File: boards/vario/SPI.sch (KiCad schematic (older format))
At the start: 21 parts, among them Q4 Q_PMOS_DGS, U1 74HC273, U2 74LS161, U3 74HC74, U31 74LS14, U32 74LS32, U33 74LS08, U4 74HC273, U5 74LS151, U6 74HC244

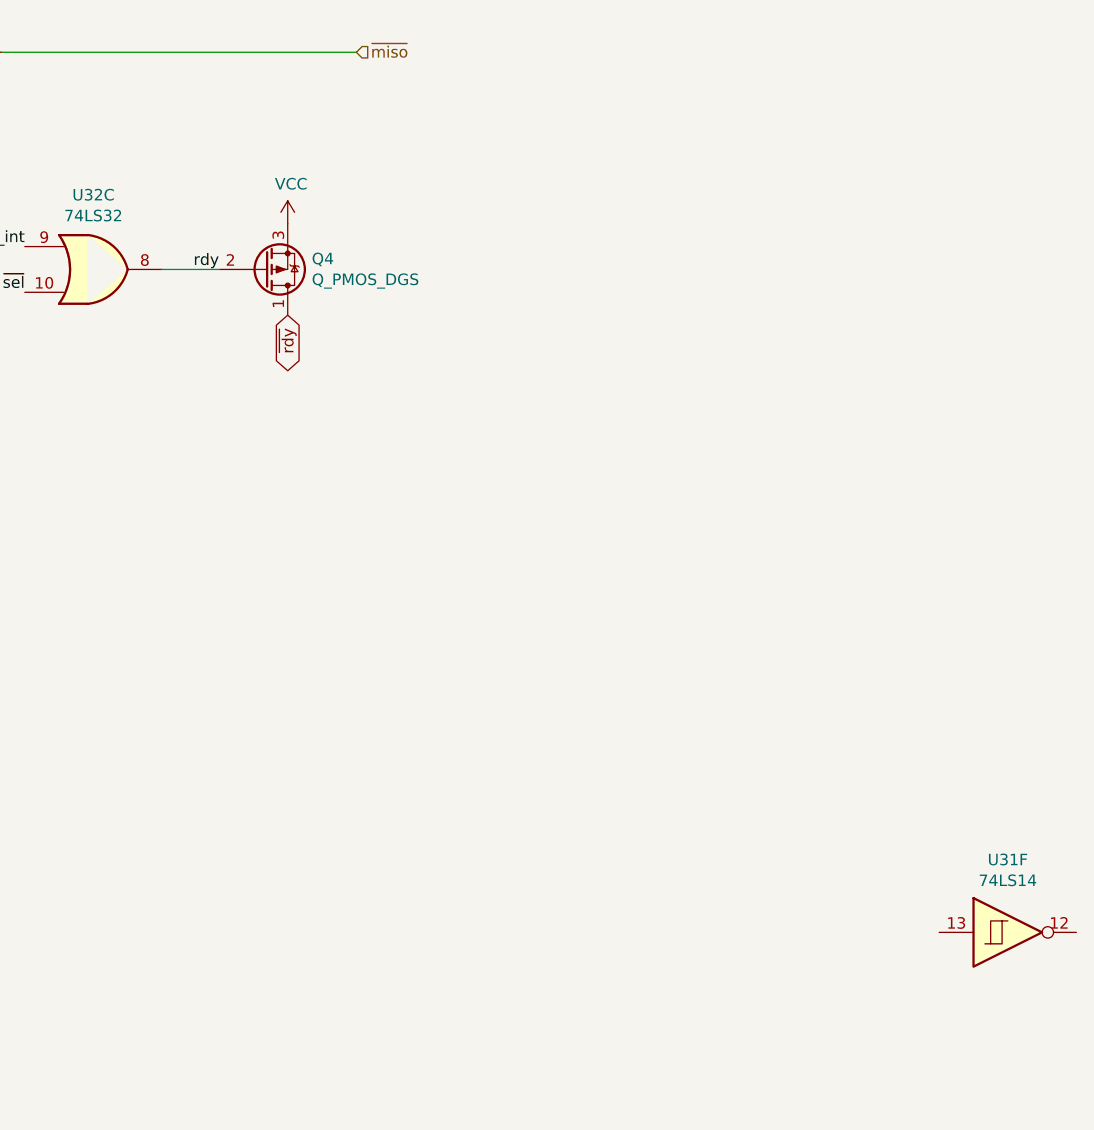
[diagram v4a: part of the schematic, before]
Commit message: SPI: invert RDY
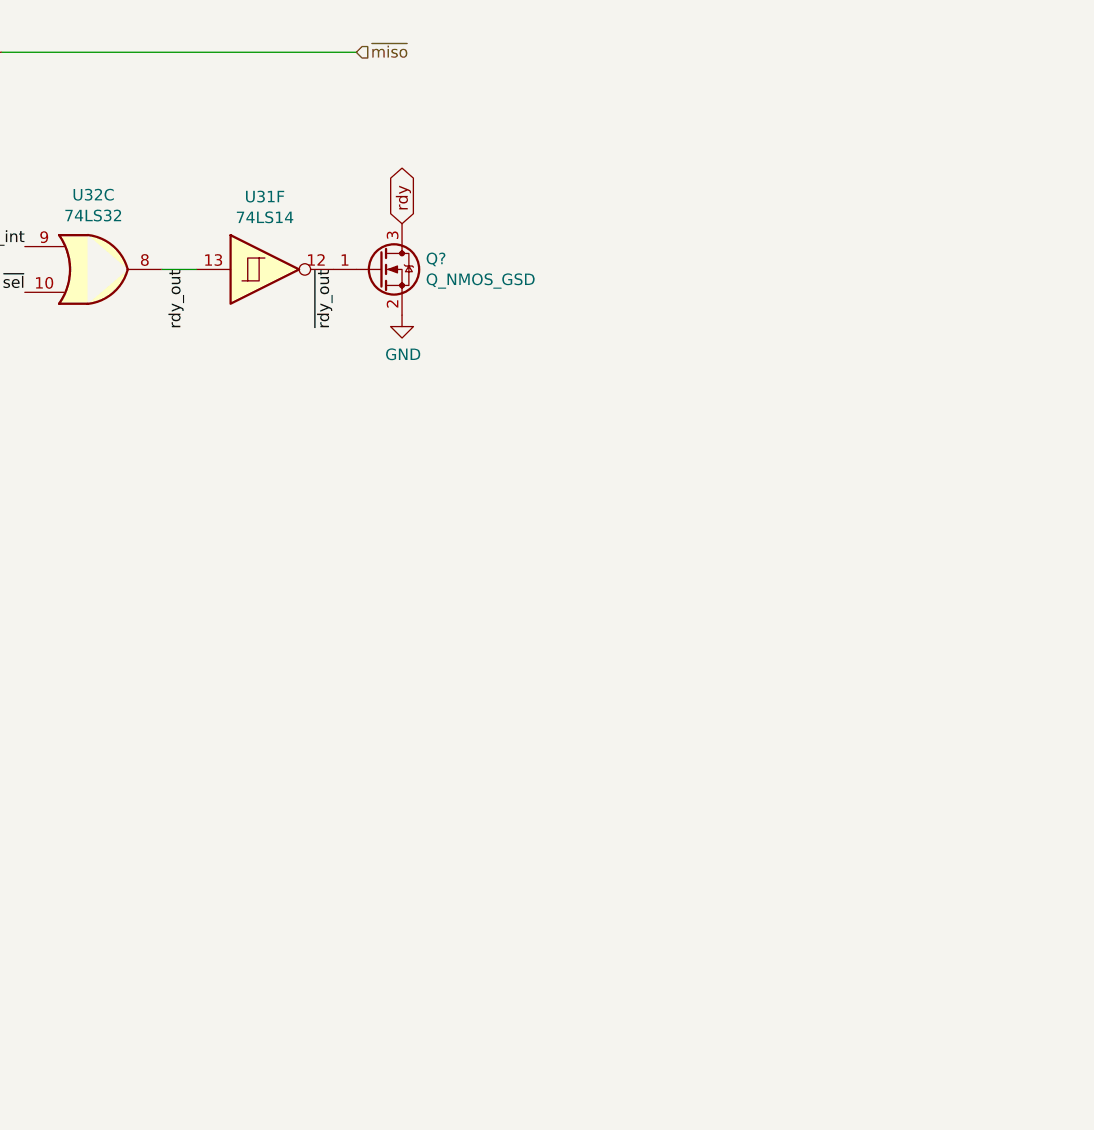
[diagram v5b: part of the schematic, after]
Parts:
- removed Q4: Q_PMOS_DGS, symbol Device:Q_PMOS_DGS
- added Q?: Q_NMOS_GSD, symbol Device:Q_NMOS_GSD
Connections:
- net GND: now also Q?.2 (S)
- net rdy: now also Q?.3 (D); no longer U32.8
- net ~rdy_out: now reaches U31.12
- net ~rdy_out: now also Q?.1 (G)
- net rdy_out: now reaches U31.13
- net rdy_out: now also U32.8
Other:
- moved on the sheet: U31F
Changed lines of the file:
@@
 	1    0    0    -1
 $EndComp
-Text GLabel 11000 4150 3    50   BiDi ~ 0
-~rdy
-$Comp
-L Device:Q_PMOS_DGS Q4
-U 1 1 604BE672
-P 10900 3950
-F 0 "Q4" H 11105 3904 50  0000 L CNN
-F 1 "Q_PMOS_DGS" H 11105 3995 50  0000 L CNN
-F 2 "" H 11100 4050 50  0001 C CNN
-F 3 "~" H 10900 3950 50  0001 C CNN
-	1    10900 3950
-	1    0    0    1
-$EndComp
-$Comp
-L power:VCC #PWR?
-U 1 1 604C2364
-P 11000 3750
-AR Path="/5FE853A4/604C2364" Ref="#PWR?"  Part="1"
-AR Path="/5FE5ABE2/604C2364" Ref="#PWR0165"  Part="1"
-F 0 "#PWR0165" H 11000 3600 50  0001 C CNN
-F 1 "VCC" H 11015 3923 50  0000 C CNN
-F 2 "" H 11000 3750 50  0001 C CNN
-F 3 "" H 11000 3750 50  0001 C CNN
-	1    11000 3750
-	1    0    0    -1
-$EndComp
-Text Label 10700 3950 2    50   ~ 0
+Text GLabel 11500 3750 1    50   BiDi ~ 0
 rdy
+Text Label 10550 3950 3    50   ~ 0
+rdy_out
 $Comp
 L 74xx:74LS14 U31
@@
 L 74xx:74LS14 U31
 U 6 1 5FEBB2AF
-P 14150 6850
-F 0 "U31" H 14150 7167 50  0000 C CNN
-F 1 "74LS14" H 14150 7076 50  0000 C CNN
-F 2 "" H 14150 6850 50  0001 C CNN
-F 3 "http://www.ti.com/lit/gpn/sn74LS14" H 14150 6850 50  0001 C CNN
-	6    14150 6850
+P 10900 3950
+F 0 "U31" H 10900 4267 50  0000 C CNN
+F 1 "74LS14" H 10900 4176 50  0000 C CNN
+F 2 "" H 10900 3950 50  0001 C CNN
+F 3 "http://www.ti.com/lit/gpn/sn74LS14" H 10900 3950 50  0001 C CNN
+	6    10900 3950
 	1    0    0    -1
 $EndComp
@@
 Text Label 9550 2500 0    50   ~ 0
 ~clk
-Wire Wire Line
-	10450 3950 10700 3950
 Text Label 9850 3850 2    50   ~ 0
 rdy_int
@@
 Wire Wire Line
 	11300 3000 9750 3000
+$Comp
+L Device:Q_NMOS_GSD Q?
+U 1 1 60205316
+P 11400 3950
+F 0 "Q?" H 11604 3996 50  0000 L CNN
+F 1 "Q_NMOS_GSD" H 11604 3905 50  0000 L CNN
+F 2 "" H 11600 4050 50  0001 C CNN
+F 3 "~" H 11400 3950 50  0001 C CNN
+	1    11400 3950
+	1    0    0    -1
+$EndComp
+$Comp
+L power:GND #PWR?
+U 1 1 60206585
+P 11500 4150
+AR Path="/5FE853A4/60206585" Ref="#PWR?"  Part="1"
+AR Path="/5FE5ABE2/60206585" Ref="#PWR?"  Part="1"
+F 0 "#PWR?" H 11500 3900 50  0001 C CNN
+F 1 "GND" H 11505 3977 50  0000 C CNN
+F 2 "" H 11500 4150 50  0001 C CNN
+F 3 "" H 11500 4150 50  0001 C CNN
+	1    11500 4150
+	1    0    0    -1
+$EndComp
+Wire Wire Line
+	10600 3950 10450 3950
 Wire Bus Line
 	1700 2050 1700 3050
+Text Label 11200 3950 3    50   ~ 0
+~rdy_out
 $EndSCHEMATC

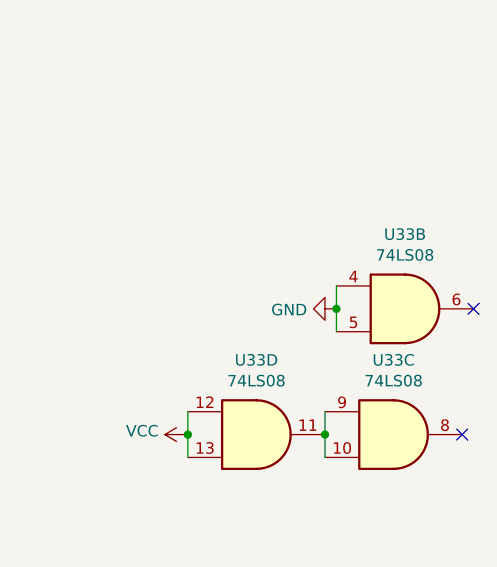
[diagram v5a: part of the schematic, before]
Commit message: PS/2: different select signals
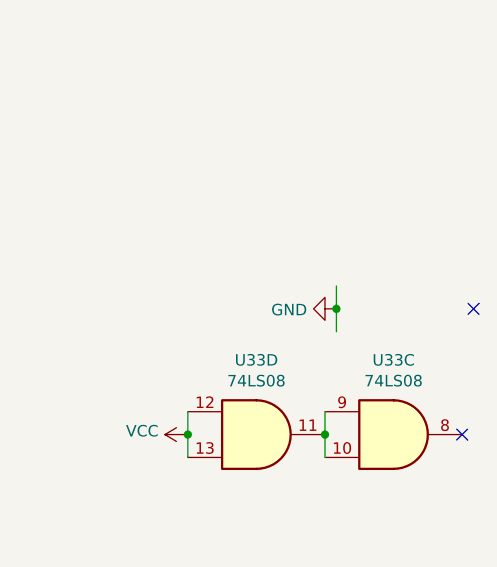
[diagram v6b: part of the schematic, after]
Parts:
- removed unit 2 of U33
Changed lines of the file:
@@
-$Comp
-L 74xx:74LS08 U33
-U 2 1 5FF1F4B8
-P 13500 8300
-F 0 "U33" H 13500 8625 50  0000 C CNN
-F 1 "74LS08" H 13500 8534 50  0000 C CNN
-F 2 "" H 13500 8300 50  0001 C CNN
-F 3 "http://www.ti.com/lit/gpn/sn74LS08" H 13500 8300 50  0001 C CNN
-	2    13500 8300
-	1    0    0    -1
-$EndComp
 $Comp
 L 74xx:74LS08 U33
@@
 Wire Wire Line
 	10600 3950 10450 3950
+Text Label 11200 3950 3    50   ~ 0
+~rdy_out
 Wire Bus Line
 	1700 2050 1700 3050
-Text Label 11200 3950 3    50   ~ 0
-~rdy_out
 $EndSCHEMATC

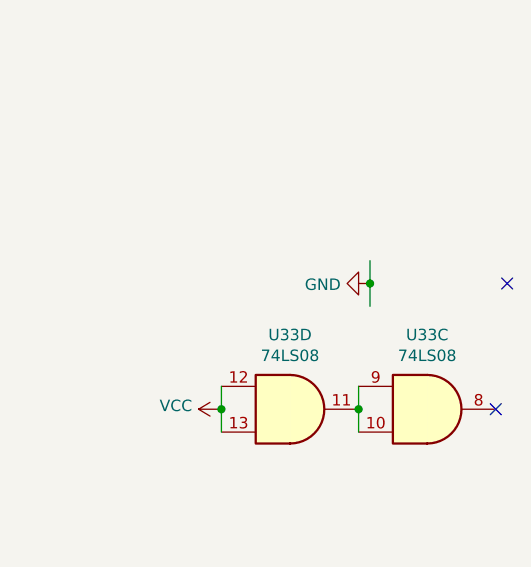
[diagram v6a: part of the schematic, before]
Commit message: Vario: address selection
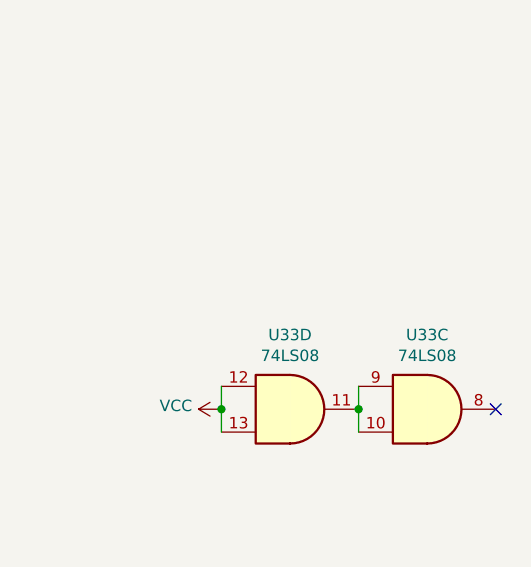
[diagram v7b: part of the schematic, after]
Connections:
- wire segments 50 -> 48
- no-connect marks 5 -> 4
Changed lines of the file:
@@
-$Comp
-L 74xx:74LS08 U33
-U 3 1 5FF20AA5
-P 13450 8850
-F 0 "U33" H 13450 9175 50  0000 C CNN
-F 1 "74LS08" H 13450 9084 50  0000 C CNN
-F 2 "" H 13450 8850 50  0001 C CNN
-F 3 "http://www.ti.com/lit/gpn/sn74LS08" H 13450 8850 50  0001 C CNN
-	3    13450 8850
-	1    0    0    -1
-$EndComp
-$Comp
-L 74xx:74LS08 U33
-U 4 1 5FF21E71
-P 12850 8850
-F 0 "U33" H 12850 9175 50  0000 C CNN
-F 1 "74LS08" H 12850 9084 50  0000 C CNN
-F 2 "" H 12850 8850 50  0001 C CNN
-F 3 "http://www.ti.com/lit/gpn/sn74LS08" H 12850 8850 50  0001 C CNN
-	4    12850 8850
-	1    0    0    -1
-$EndComp
 $Comp
 L 74xx:74LS08 U33
@@
 	1    0    0    -1
 $EndComp
-Wire Wire Line
-	13150 8750 13150 8850
-Connection ~ 13150 8850
-Wire Wire Line
-	13150 8850 13150 8950
-Wire Wire Line
-	12550 8750 12550 8850
+NoConn ~ 6750 8500
+Wire Wire Line
+	11300 3000 9750 3000
+$Comp
+L Device:Q_NMOS_GSD Q?
+U 1 1 60205316
+P 11400 3950
+F 0 "Q?" H 11604 3996 50  0000 L CNN
+F 1 "Q_NMOS_GSD" H 11604 3905 50  0000 L CNN
+F 2 "" H 11600 4050 50  0001 C CNN
+F 3 "~" H 11400 3950 50  0001 C CNN
+	1    11400 3950
+	1    0    0    -1
+$EndComp
+$Comp
+L power:GND #PWR?
+U 1 1 60206585
+P 11500 4150
+AR Path="/5FE853A4/60206585" Ref="#PWR?"  Part="1"
+AR Path="/5FE5ABE2/60206585" Ref="#PWR?"  Part="1"
+F 0 "#PWR?" H 11500 3900 50  0001 C CNN
+F 1 "GND" H 11505 3977 50  0000 C CNN
+F 2 "" H 11500 4150 50  0001 C CNN
+F 3 "" H 11500 4150 50  0001 C CNN
+	1    11500 4150
+	1    0    0    -1
+$EndComp
+Wire Wire Line
+	10600 3950 10450 3950
+Text Label 11200 3950 3    50   ~ 0
+~rdy_out
+Wire Bus Line
+	1700 2050 1700 3050
+NoConn ~ 13750 8850
+Wire Wire Line
+	12550 8850 12550 8950
 $Comp
 L power:VCC #PWR?
@@
 Connection ~ 12550 8850
 Wire Wire Line
-	12550 8850 12550 8950
-$Comp
-L power:GND #PWR?
-U 1 1 5FF6B270
-P 13200 8300
-AR Path="/5FF6B270" Ref="#PWR?"  Part="1"
-AR Path="/5FE5ABE2/5FF6B270" Ref="#PWR0180"  Part="1"
-F 0 "#PWR0180" H 13200 8050 50  0001 C CNN
-F 1 "GND" V 13205 8172 50  0000 R CNN
-F 2 "" H 13200 8300 50  0001 C CNN
-F 3 "" H 13200 8300 50  0001 C CNN
-	1    13200 8300
-	0    1    1    0
-$EndComp
-Wire Wire Line
-	13200 8400 13200 8300
-Connection ~ 13200 8300
-Wire Wire Line
-	13200 8300 13200 8200
-NoConn ~ 13800 8300
-NoConn ~ 13750 8850
-NoConn ~ 6750 8500
-Wire Wire Line
-	11300 3000 9750 3000
-$Comp
-L Device:Q_NMOS_GSD Q?
-U 1 1 60205316
-P 11400 3950
-F 0 "Q?" H 11604 3996 50  0000 L CNN
-F 1 "Q_NMOS_GSD" H 11604 3905 50  0000 L CNN
-F 2 "" H 11600 4050 50  0001 C CNN
-F 3 "~" H 11400 3950 50  0001 C CNN
-	1    11400 3950
-	1    0    0    -1
-$EndComp
-$Comp
-L power:GND #PWR?
-U 1 1 60206585
-P 11500 4150
-AR Path="/5FE853A4/60206585" Ref="#PWR?"  Part="1"
-AR Path="/5FE5ABE2/60206585" Ref="#PWR?"  Part="1"
-F 0 "#PWR?" H 11500 3900 50  0001 C CNN
-F 1 "GND" H 11505 3977 50  0000 C CNN
-F 2 "" H 11500 4150 50  0001 C CNN
-F 3 "" H 11500 4150 50  0001 C CNN
-	1    11500 4150
-	1    0    0    -1
-$EndComp
-Wire Wire Line
-	10600 3950 10450 3950
-Text Label 11200 3950 3    50   ~ 0
-~rdy_out
-Wire Bus Line
-	1700 2050 1700 3050
+	12550 8750 12550 8850
+Wire Wire Line
+	13150 8850 13150 8950
+Wire Wire Line
+	13150 8750 13150 8850
+Connection ~ 13150 8850
+$Comp
+L 74xx:74LS08 U33
+U 4 1 5FF21E71
+P 12850 8850
+F 0 "U33" H 12850 9175 50  0000 C CNN
+F 1 "74LS08" H 12850 9084 50  0000 C CNN
+F 2 "" H 12850 8850 50  0001 C CNN
+F 3 "http://www.ti.com/lit/gpn/sn74LS08" H 12850 8850 50  0001 C CNN
+	4    12850 8850
+	1    0    0    -1
+$EndComp
+$Comp
+L 74xx:74LS08 U33
+U 3 1 5FF20AA5
+P 13450 8850
+F 0 "U33" H 13450 9175 50  0000 C CNN
+F 1 "74LS08" H 13450 9084 50  0000 C CNN
+F 2 "" H 13450 8850 50  0001 C CNN
+F 3 "http://www.ti.com/lit/gpn/sn74LS08" H 13450 8850 50  0001 C CNN
+	3    13450 8850
+	1    0    0    -1
+$EndComp
 $EndSCHEMATC

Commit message: Vario: status LEDs
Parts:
- added D2: LED, symbol Device:LED
- added R19: 620, symbol Device:R
- gave numbers to parts that had none: 1
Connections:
- net GND: now also R19.1
- net clk_ena: now also D2.2 (A)
- new net: D2.1 (K), R19.2
- no-connect marks 4 -> 3
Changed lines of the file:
@@
 	1    0    0    -1
 $EndComp
-NoConn ~ 6750 8500
 Wire Wire Line
 	11300 3000 9750 3000
 $Comp
-L Device:Q_NMOS_GSD Q?
+L Device:Q_NMOS_GSD Q2
 U 1 1 60205316
 P 11400 3950
-F 0 "Q?" H 11604 3996 50  0000 L CNN
+F 0 "Q2" H 11604 3996 50  0000 L CNN
 F 1 "Q_NMOS_GSD" H 11604 3905 50  0000 L CNN
 F 2 "" H 11600 4050 50  0001 C CNN
@@
 P 11500 4150
 AR Path="/5FE853A4/60206585" Ref="#PWR?"  Part="1"
-AR Path="/5FE5ABE2/60206585" Ref="#PWR?"  Part="1"
-F 0 "#PWR?" H 11500 3900 50  0001 C CNN
+AR Path="/5FE5ABE2/60206585" Ref="#PWR0225"  Part="1"
+F 0 "#PWR0225" H 11500 3900 50  0001 C CNN
 F 1 "GND" H 11505 3977 50  0000 C CNN
 F 2 "" H 11500 4150 50  0001 C CNN
@@
 Text Label 11200 3950 3    50   ~ 0
 ~rdy_out
-Wire Bus Line
-	1700 2050 1700 3050
 NoConn ~ 13750 8850
 Wire Wire Line
@@
 	1    0    0    -1
 $EndComp
+$Comp
+L Device:LED D2
+U 1 1 60392BD3
+P 7400 8500
+F 0 "D2" H 7393 8245 50  0000 C CNN
+F 1 "LED" H 7393 8336 50  0000 C CNN
+F 2 "" H 7400 8500 50  0001 C CNN
+F 3 "~" H 7400 8500 50  0001 C CNN
+	1    7400 8500
+	-1   0    0    1
+$EndComp
+Wire Wire Line
+	6750 8500 7250 8500
+Wire Bus Line
+	1700 2050 1700 3050
+$Comp
+L Device:R R19
+U 1 1 60397E60
+P 7700 8500
+F 0 "R19" V 7493 8500 50  0000 C CNN
+F 1 "620" V 7584 8500 50  0000 C CNN
+F 2 "" V 7630 8500 50  0001 C CNN
+F 3 "~" H 7700 8500 50  0001 C CNN
+	1    7700 8500
+	0    1    1    0
+$EndComp
+$Comp
+L power:GND #PWR?
+U 1 1 603983EF
+P 7850 8500
+AR Path="/603983EF" Ref="#PWR?"  Part="1"
+AR Path="/5FE5ABE2/603983EF" Ref="#PWR0224"  Part="1"
+F 0 "#PWR0224" H 7850 8250 50  0001 C CNN
+F 1 "GND" V 7855 8372 50  0000 R CNN
+F 2 "" H 7850 8500 50  0001 C CNN
+F 3 "" H 7850 8500 50  0001 C CNN
+	1    7850 8500
+	0    -1   -1   0
+$EndComp
 $EndSCHEMATC
